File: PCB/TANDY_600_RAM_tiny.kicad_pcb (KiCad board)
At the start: 2 copper layers, 68.6 x 16.5 mm, 5 parts, among them J1 DIN 41612 2x22 male right-ang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, U1 628128_TSOP, U2 74HC08

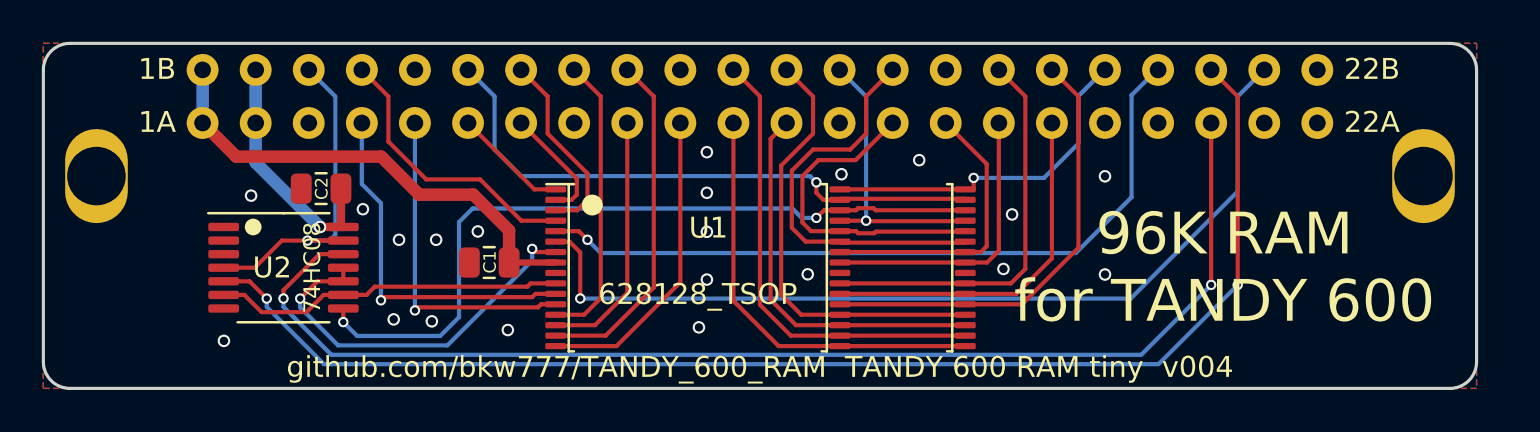
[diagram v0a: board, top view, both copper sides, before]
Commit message: gnd on tiny, new dual sch, bus connector symbol & footprint
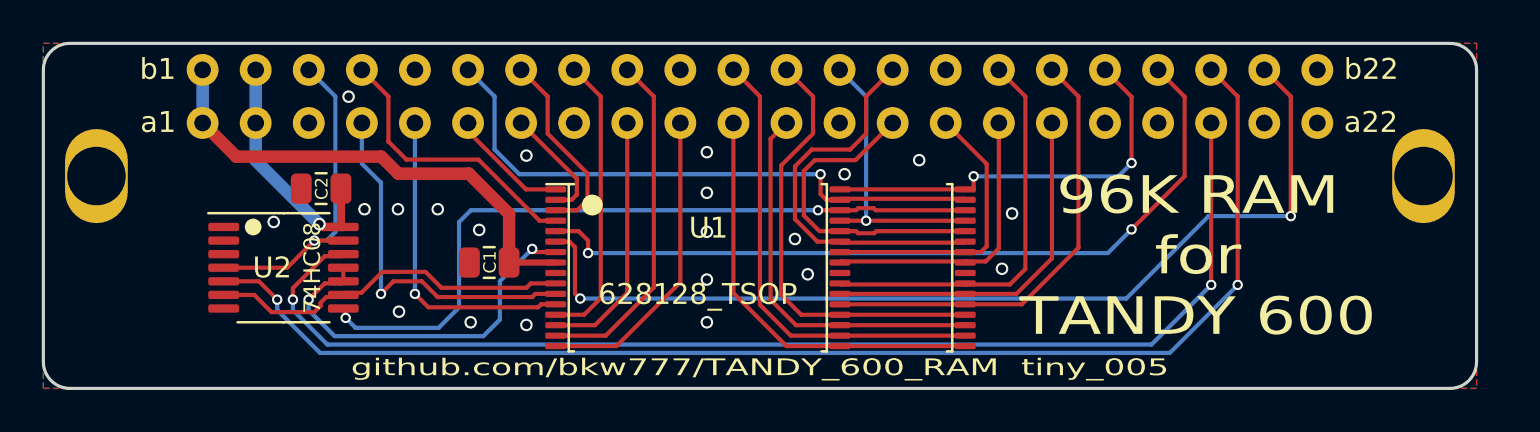
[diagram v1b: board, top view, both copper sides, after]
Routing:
- net /CS2: track 43.5 -> 46.8 mm, vias 1 -> 2
- net /~{OE}: track 16.7 -> 19.8 mm, vias 1 -> 2
- net /~{WE}: track 35.8 -> 38.0 mm, vias 1 -> 2
- net /~{CS1_C}: track 58.8 -> 57.7 mm
- net /~{CS1}: track 36.3 -> 35.1 mm
- net /A16: track 16.8 -> 17.5 mm
- net /A12: track 15.8 -> 15.2 mm
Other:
- board text added: "${COMMENT2} ${REVISION}"
- board text added: "a1"
- board text added: "a22"
- board text added: "b1"
- board text added: "b22"
- board text removed: "${COMMENT2} ${TITLE} v${REVISION}"
- board text removed: "1A"
- board text removed: "1B"
- board text removed: "22A"
- board text removed: "22B"

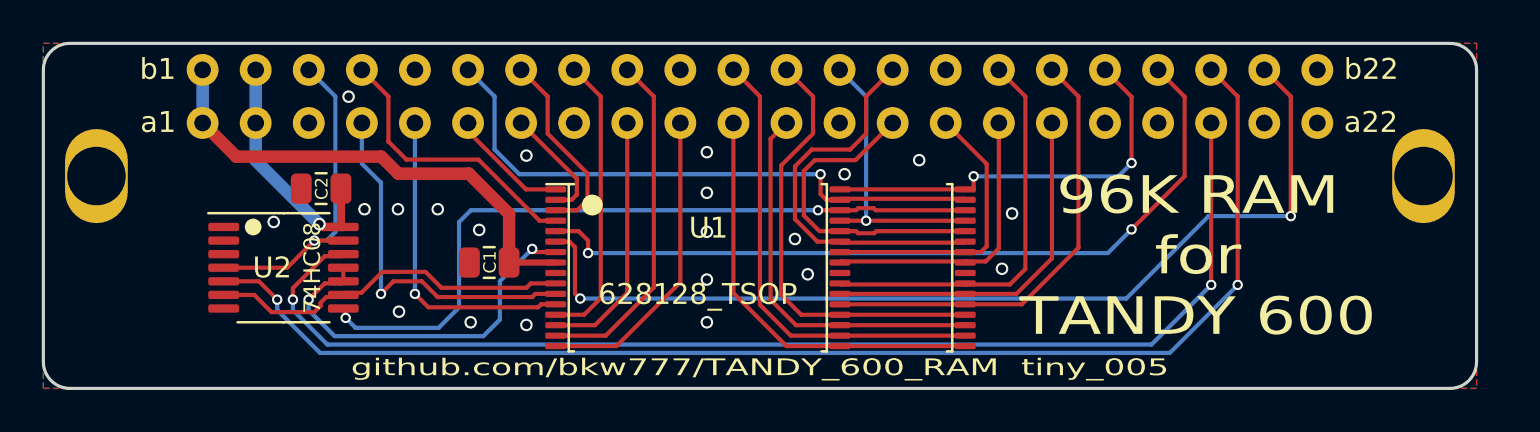
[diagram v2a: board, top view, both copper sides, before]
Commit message: footprints, ground paths
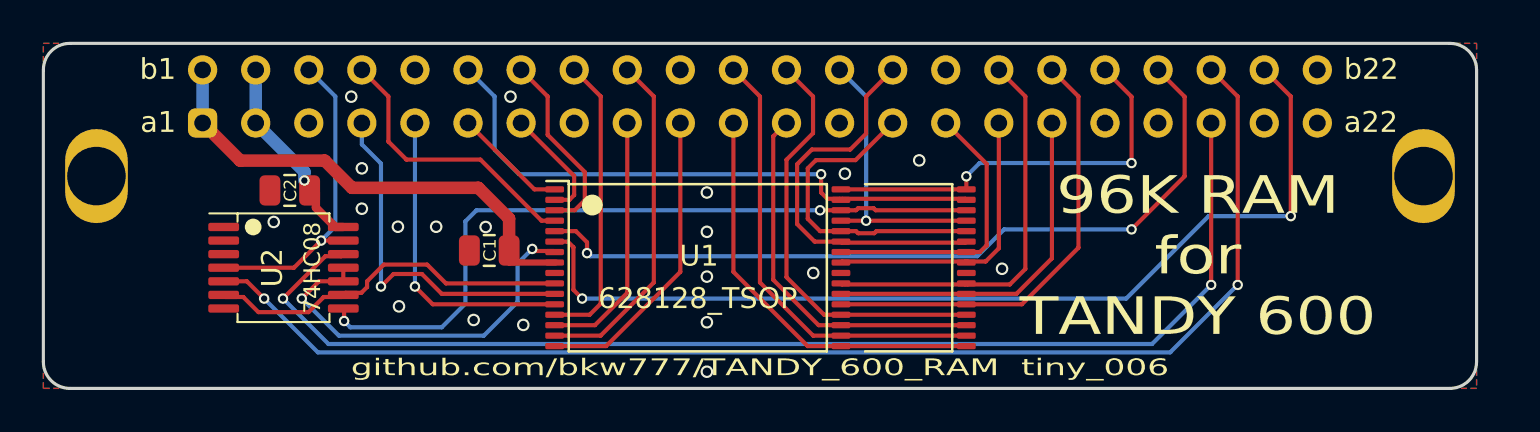
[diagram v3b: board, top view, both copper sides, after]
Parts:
- J1: footprint 000_LOCAL:DIN 41612 2x22 male right-angle -> 000_LOCAL:DIN-41612_02x22_male_horizontal
- moved C2 1.50 mm to (123.5, 106.0)
- moved C1 0.58 mm to (133.1, 108.9)
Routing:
- net VCC: track 11.7 -> 9.48 mm
- net /A0: track 21.1 -> 20.3 mm
- net /A1: track 18.6 -> 17.9 mm
- net /A2: track 22.2 -> 21.6 mm
- net /A3: track 20.3 -> 19.7 mm
- net GND: vias 21 -> 20

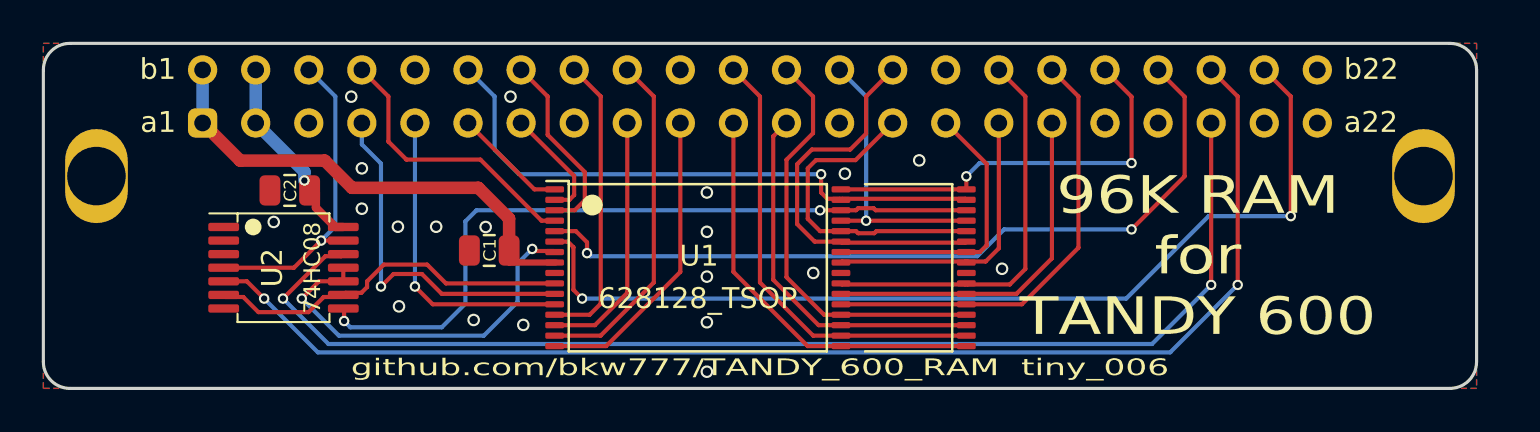
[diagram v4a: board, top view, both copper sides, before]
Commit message: footprints on tiny
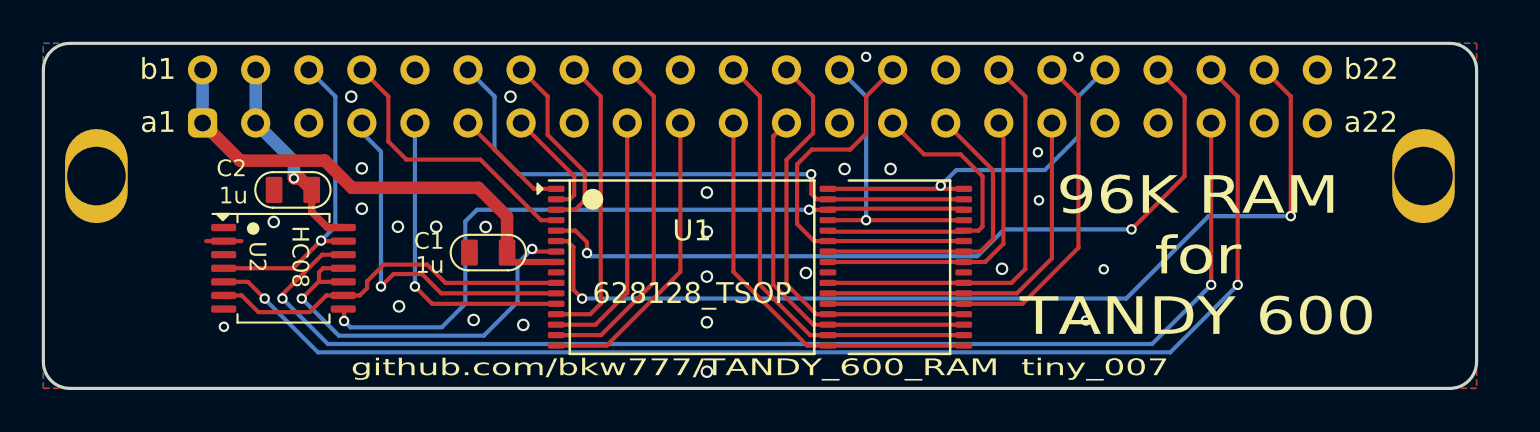
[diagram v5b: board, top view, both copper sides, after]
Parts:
- C1, C2: value 0.1uF -> 1u
- U2: value 74HC08 -> HC08
- moved U1 3.28 mm to (142.8, 109.7)
- moved C2 0.15 mm to (123.7, 106.0)
- moved C1 0.11 mm to (133.1, 109.0)
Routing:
- net /~{OE}: track 19.8 -> 17.9 mm, vias 2 -> 1
- net GND: track 0.00 -> 1.70 mm, vias 20 -> 27
- net /A15: track 18.7 -> 19.8 mm
- net /D4: track 13.8 -> 14.6 mm
- net /D3: track 13.9 -> 14.6 mm
- net /D1: track 17.3 -> 17.9 mm
- net /D0: track 21.5 -> 22.1 mm
- net /D2: track 19.2 -> 19.8 mm
- net /D7: track 13.7 -> 14.3 mm

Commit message: rename 3d dir to 3dshapes to standardize
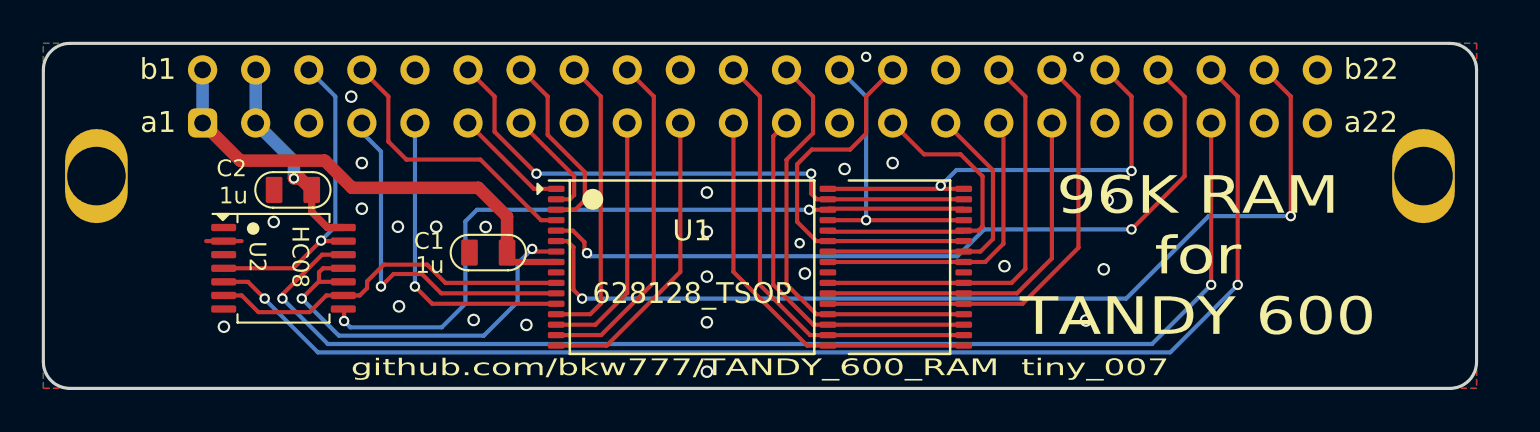
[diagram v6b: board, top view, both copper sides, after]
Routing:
- net /~{OE}: track 17.9 -> 21.4 mm, vias 1 -> 2
- net /A10: track 28.3 -> 27.9 mm, vias 1 -> 2
- net GND: vias 27 -> 26
